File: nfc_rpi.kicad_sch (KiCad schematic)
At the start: 0 parts

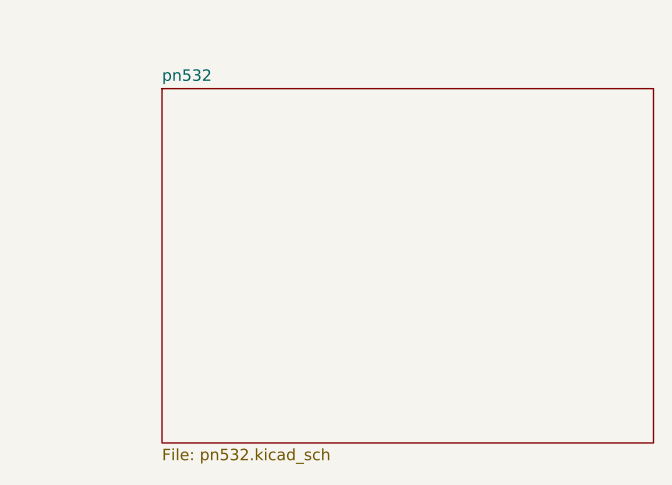
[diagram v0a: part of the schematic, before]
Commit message: Add hierarchical pins for Raspberry Pi connector
- Added hierarchical labels in raspberry_pn532.kicad_sch for connected J1 pins
- Added hierarchical pins on raspberry sheet in nfc.kicad_sch
- Pins: SDA, SCL, GPIO5, GPIO6, MISO, SCK, 5V, GND
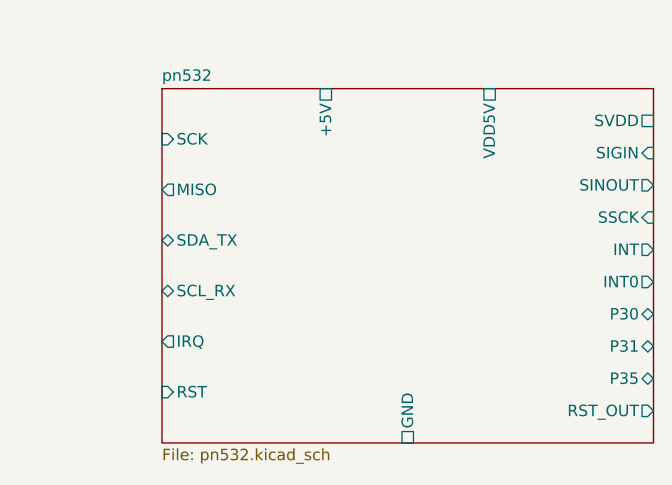
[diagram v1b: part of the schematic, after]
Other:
- sheet pn532 ports: added +5V, GND, INT, INT0, IRQ, MISO, P30, P31, P35, RST, RST_OUT, SCK, SCL_RX, SDA_TX, SIGIN, SINOUT, SSCK, SVDD, VDD5V; removed none
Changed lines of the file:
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@@
+			)
+		)
+		(pin "SCK" input
+			(at 186.69 69.12 180)
+			(effects
+				(font
+					(size 1.27 1.27)
+				)
+			)
+		)
+		(pin "MISO" output
+			(at 186.69 74.74 180)
+			(effects
+				(font
+					(size 1.27 1.27)
+				)
+			)
+		)
+		(pin "SDA_TX" bidirectional
+			(at 186.69 80.36 180)
+			(effects
+				(font
+					(size 1.27 1.27)
+				)
+			)
+		)
+		(pin "SCL_RX" bidirectional
+			(at 186.69 85.98 180)
+			(effects
+				(font
+					(size 1.27 1.27)
+				)
+			)
+		)
+		(pin "IRQ" output
+			(at 186.69 91.60 180)
+			(effects
+				(font
+					(size 1.27 1.27)
+				)
+			)
+		)
+		(pin "RST" input
+			(at 186.69 97.22 180)
+			(effects
+				(font
+					(size 1.27 1.27)
+				)
+			)
+		)
+		(pin "+5V" passive
+			(at 204.89 63.5 90)
+			(effects
+				(font
+					(size 1.27 1.27)
+				)
+			)
+		)
+		(pin "VDD5V" passive
+			(at 223.09 63.5 90)
+			(effects
+				(font
+					(size 1.27 1.27)
+				)
+			)
+		)
+		(pin "GND" passive
+			(at 213.995 102.87 270)
+			(effects
+				(font
+					(size 1.27 1.27)
+				)
+			)
+		)
+		(pin "SVDD" passive
+			(at 241.3 67.08 0)
+			(effects
+				(font
+					(size 1.27 1.27)
+				)
+			)
+		)
+		(pin "SIGIN" input
+			(at 241.3 70.66 0)
+			(effects
+				(font
+					(size 1.27 1.27)
+				)
+			)
+		)
+		(pin "SINOUT" output
+			(at 241.3 74.24 0)
+			(effects
+				(font
+					(size 1.27 1.27)
+				)
+			)
+		)
+		(pin "SSCK" input
+			(at 241.3 77.82 0)
+			(effects
+				(font
+					(size 1.27 1.27)
+				)
+			)
+		)
+		(pin "INT" output
+			(at 241.3 81.40 0)
+			(effects
+				(font
+					(size 1.27 1.27)
+				)
+			)
+		)
+		(pin "INT0" output
+			(at 241.3 84.98 0)
+			(effects
+				(font
+					(size 1.27 1.27)
+				)
+			)
+		)
+		(pin "P30" bidirectional
+			(at 241.3 88.56 0)
+			(effects
+				(font
+					(size 1.27 1.27)
+				)
+			)
+		)
+		(pin "P31" bidirectional
+			(at 241.3 92.14 0)
+			(effects
+				(font
+					(size 1.27 1.27)
+				)
+			)
+		)
+		(pin "P35" bidirectional
+			(at 241.3 95.72 0)
+			(effects
+				(font
+					(size 1.27 1.27)
+				)
+			)
+		)
+		(pin "RST_OUT" output
+			(at 241.3 99.30 0)
+			(effects
+				(font
+					(size 1.27 1.27)
+				)
 			)
 		)

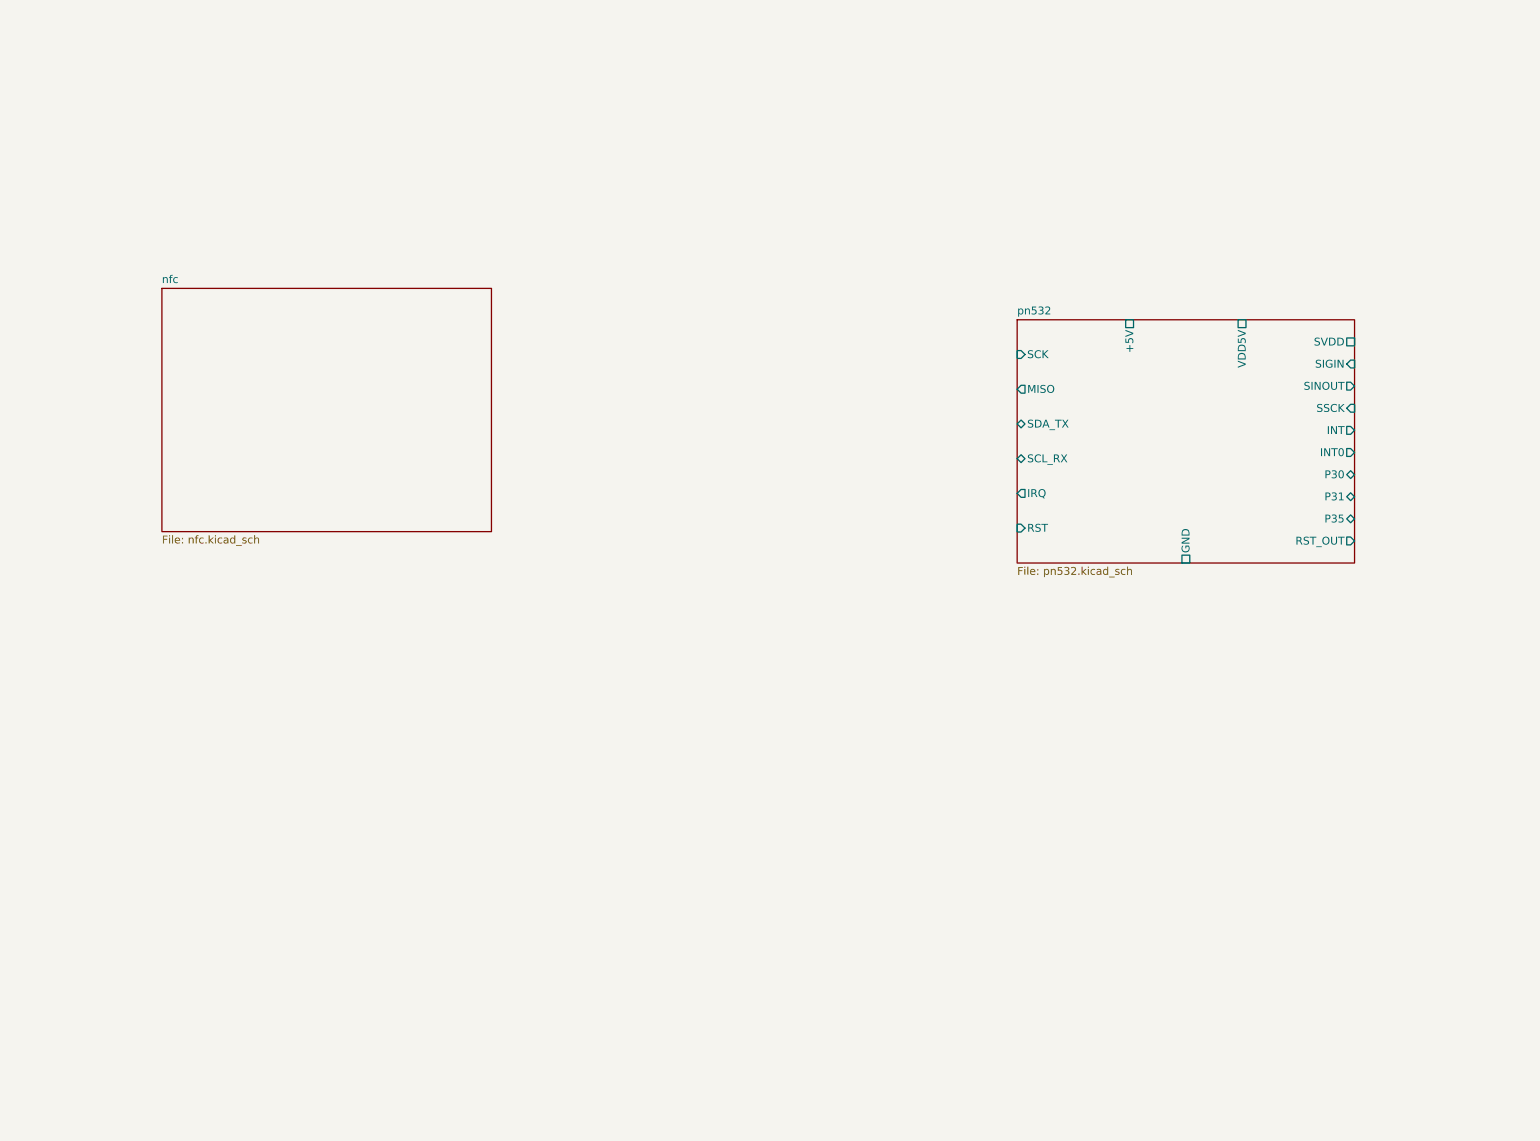
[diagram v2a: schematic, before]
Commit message: Rename Raspberry sheet, enlarge to 120x250mm, 5mm pin spacing
- Sheet name: 'raspberry (page 4)' -> 'Raspberry'
- Sheet size: 49.53x38.1 -> 120x250mm
- 26 left pins, 27 right pins with 5mm spacing
- No GND/power pins (removed in prior commits)
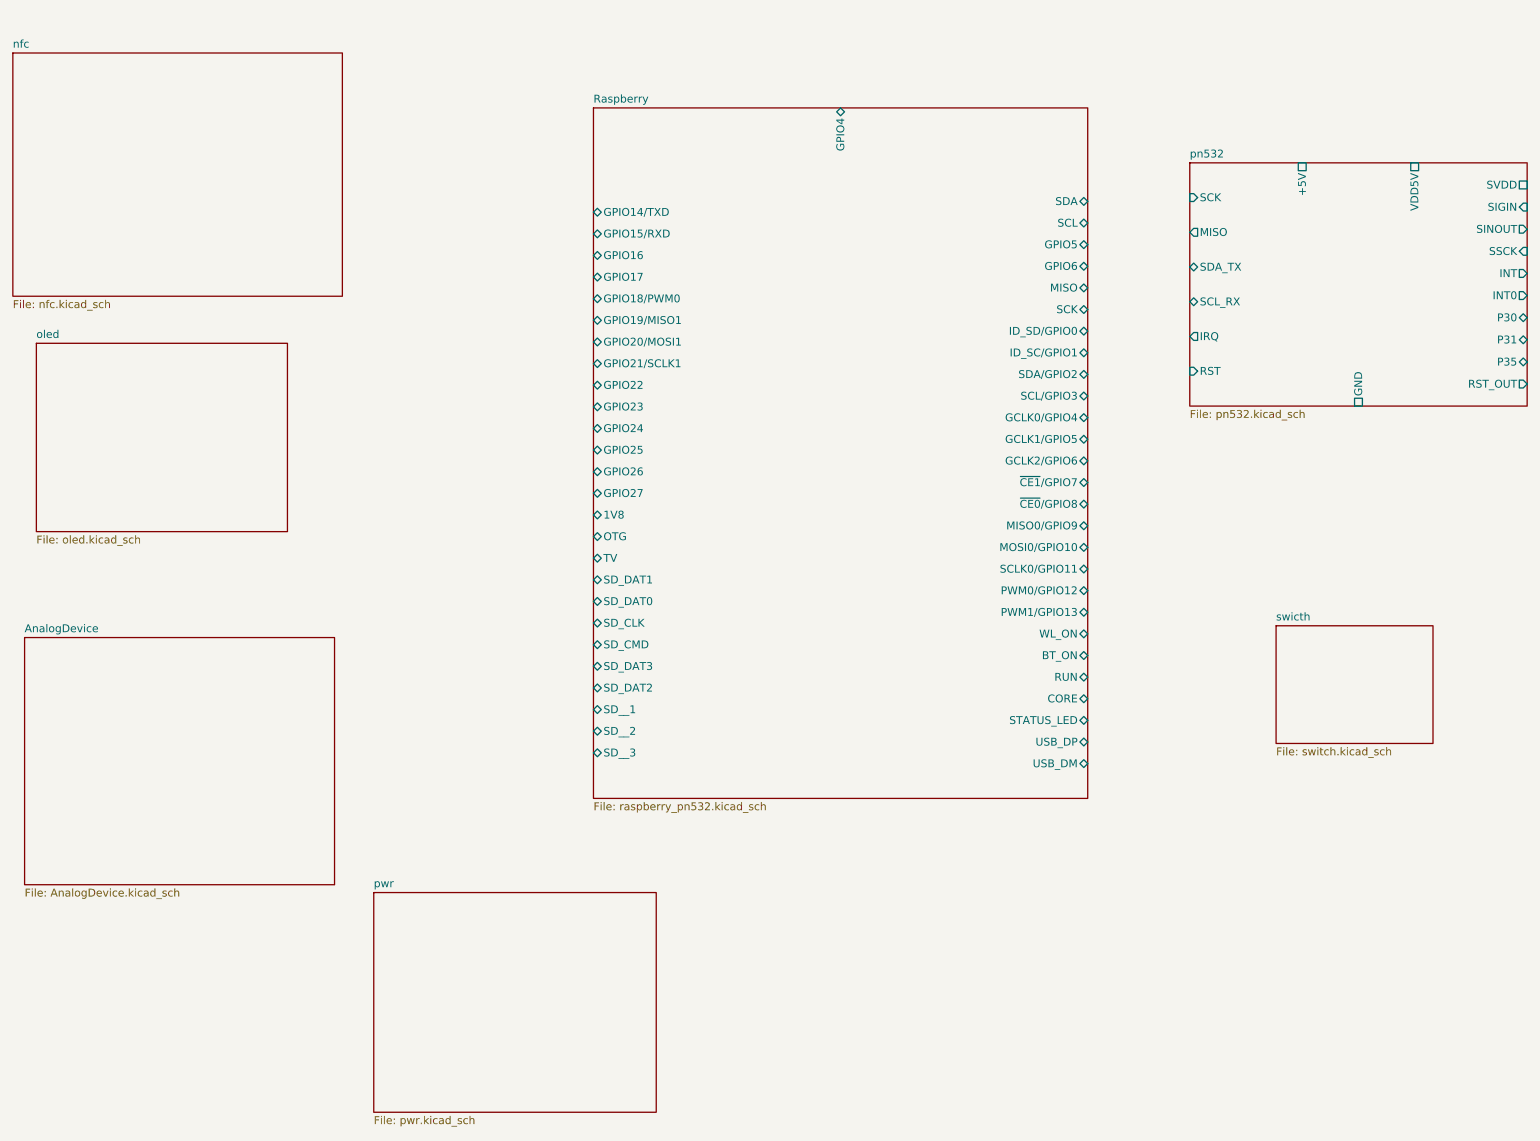
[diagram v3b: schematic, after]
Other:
- added sheet AnalogDevice (AnalogDevice.kicad_sch)
- added sheet Raspberry (raspberry_pn532.kicad_sch)
- added sheet oled (oled.kicad_sch)
- added sheet pwr (pwr.kicad_sch)
- added sheet swicth (switch.kicad_sch)

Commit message: Add hierarchical labels/pins across all sheets, fix DiscoveryAnalog3 rename, PCB 99x99mm rounded corners
- nfc_rpi.kicad_sch: 19 hierarchical pins on PN532 sheet
- pn532.kicad_sch: 22 hierarchical labels with _PN532 suffix
- raspberry_pn532.kicad_sch: 68 hierarchical labels for J1
- nfc.kicad_sch: 54 signal pins on Raspberry sheet, power pins removed
- switch.kicad_sch: 8 switch+resistor circuits with hierarchical labels
- oled.kicad_sch: 7 hierarchical labels
- DiscoveryAnalog3.kicad_sch: 26 hierarchical labels for J4 connector
- nfc_rpi.kicad_pcb: 99x99mm board outline with 5mm rounded corners (gr_line + gr_arc)
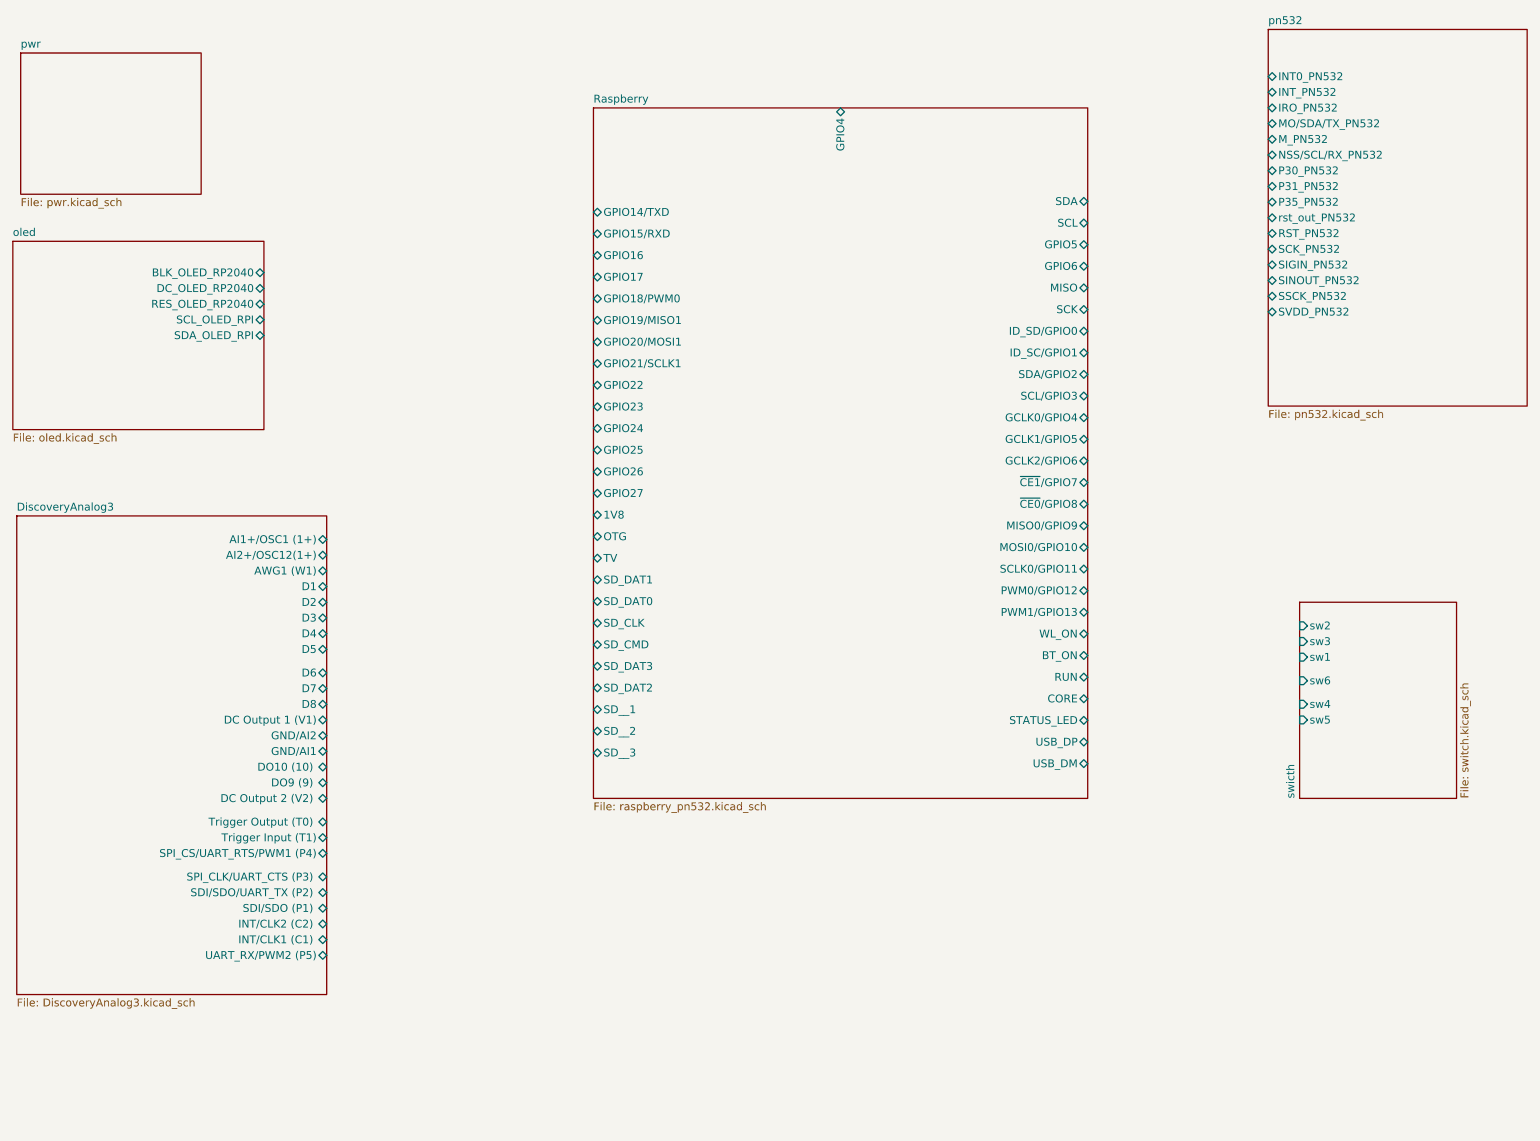
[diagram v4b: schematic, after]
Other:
- sheet AnalogDevice renamed DiscoveryAnalog3
- removed sheet nfc
- sheet DiscoveryAnalog3: file AnalogDevice.kicad_sch -> DiscoveryAnalog3.kicad_sch
- sheet DiscoveryAnalog3 ports: added AI1+/OSC1 (1+), AI2+/OSC12(1+), AWG1 (W1), D1, D2, D3, D4, D5, D6, D7, D8, DC Output 1 (V1), DC Output 2 (V2) , DO10 (10) , DO9 (9) , GND/AI1, GND/AI2, INT/CLK1 (C1) , INT/CLK2 (C2) , SDI/SDO (P1) , SDI/SDO/UART_TX (P2) , SPI_CLK/UART_CTS (P3) , SPI_CS/UART_RTS/PWM1 (P4), Trigger Input (T1), Trigger Output (T0) , UART_RX/PWM2 (P5); removed none
- sheet oled ports: added BLK_OLED_RP2040, DC_OLED_RP2040, RES_OLED_RP2040, SCL_OLED_RPI, SDA_OLED_RPI; removed none
- sheet pn532 ports: added INT0_PN532, INT_PN532, IRO_PN532, MO/SDA/TX_PN532, M_PN532, NSS/SCL/RX_PN532, P30_PN532, P31_PN532, P35_PN532, RST_PN532, SCK_PN532, SIGIN_PN532, SINOUT_PN532, SSCK_PN532, SVDD_PN532, rst_out_PN532; removed +5V, GND, INT, INT0, IRQ, MISO, P30, P31, P35, RST, RST_OUT, SCK, SCL_RX, SDA_TX, SIGIN, SINOUT, SSCK, SVDD, VDD5V
- sheet swicth ports: added sw1, sw2, sw3, sw4, sw5, sw6; removed none
